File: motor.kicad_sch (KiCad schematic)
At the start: 6 parts, among them IC3 DRV8300DPWR, Q1 Q_NMOS

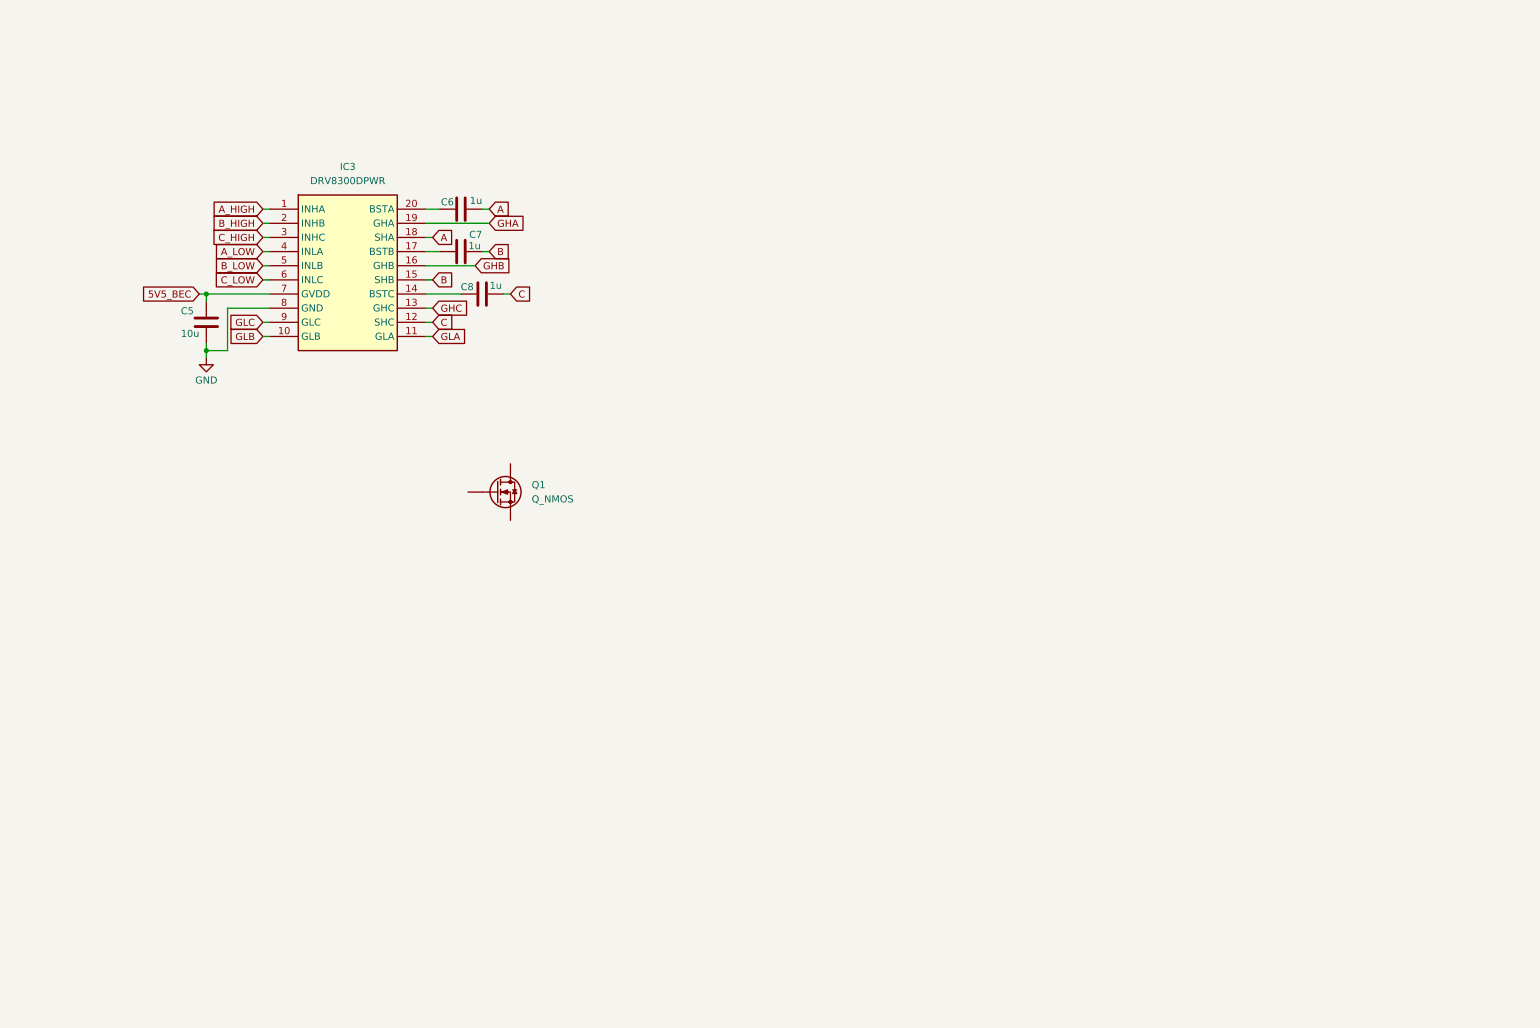
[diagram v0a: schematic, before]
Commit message: finished one full channel, still to duplicate this for 4 channels esc
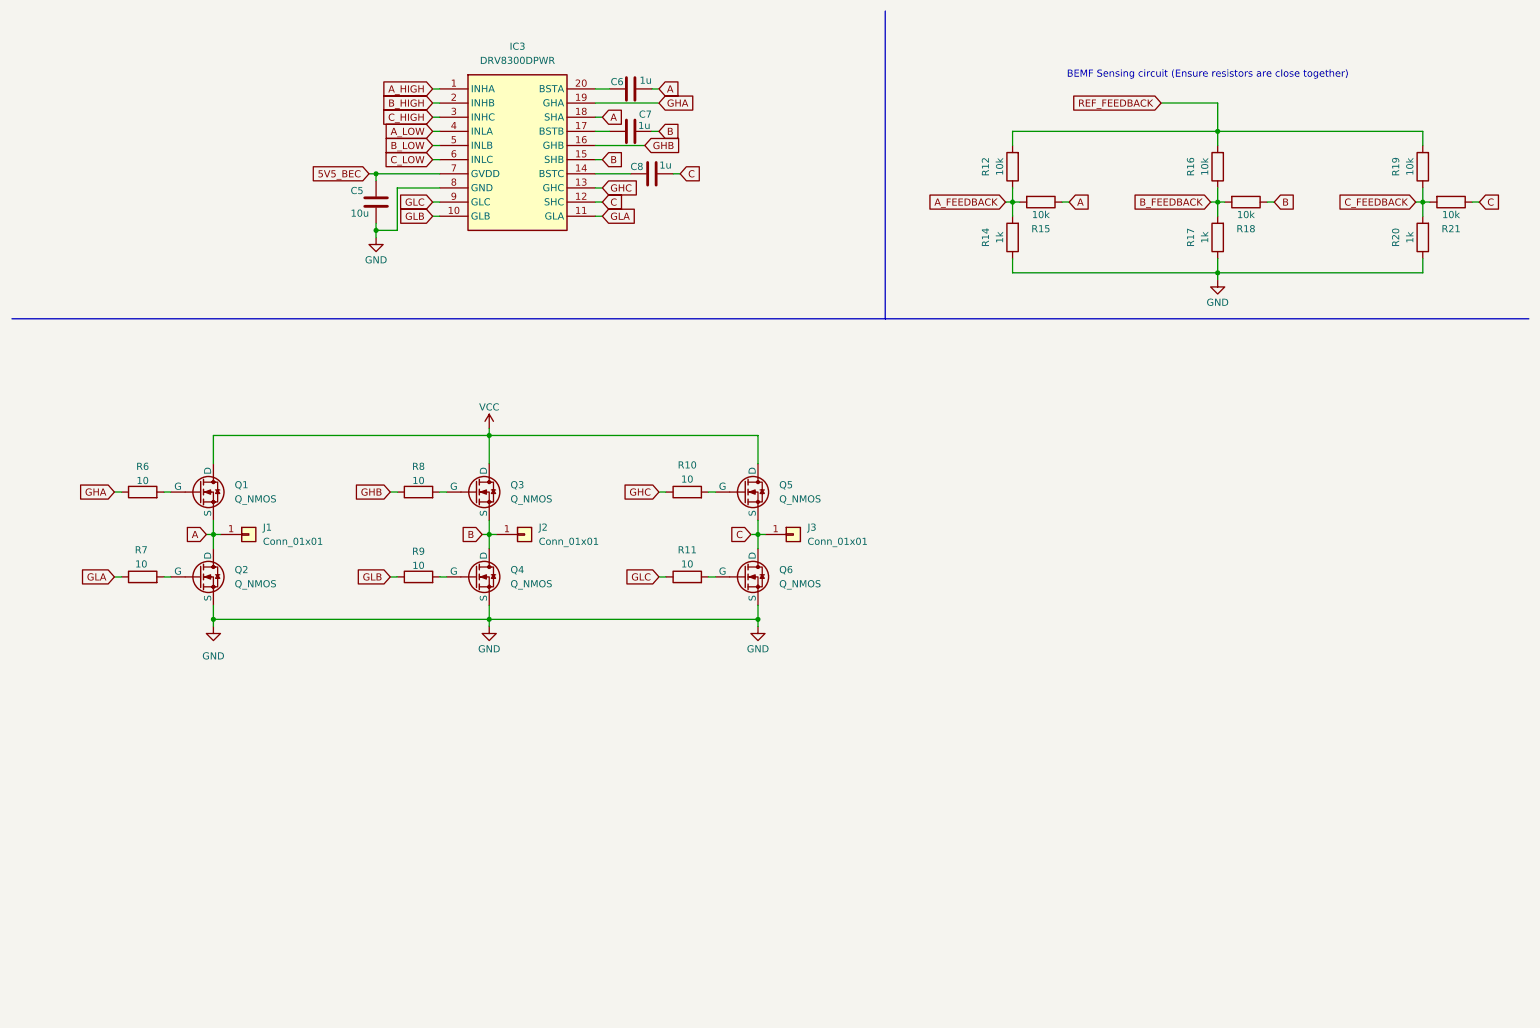
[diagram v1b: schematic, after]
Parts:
- added J1, J2, J3: Conn_01x01, symbol Connector_Generic:Conn_01x01
- added Q2, Q3, Q4, Q5, Q6: Q_NMOS, symbol Device:Q_NMOS
- added R10, R11, R6, R7, R8, R9: 10, symbol Device:R
- added R12, R15, R16, R18, R19, R21: 10k, symbol Device:R
- added R14, R17, R20: 1k, symbol Device:R
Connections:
- net A: now also Q1.S, J1.1 (Pin_1), Q2.D, R15.1
- net B: now also J2.1 (Pin_1), Q3.S, Q4.D, R18.1
- net C: now also J3.1 (Pin_1), Q5.S, Q6.D, R21.1
- net GHA: now also R6.1
- net GHB: now also R8.1
- net GHC: now also R10.1
- net GLA: now also R7.1
- net GLB: now also R9.1
- net GLC: now also R11.1
- net GND: now also Q2.S, Q4.S, Q6.S, R14.1, R17.1, R20.1
- net VCC: now reaches Q1.D
- net VCC: now also Q3.D, Q5.D
- net at Q1.G: now also R6.2
- new net: Q5.G, R10.2
- new net: Q4.G, R9.2
- new net: Q3.G, R8.2
- new net: Q6.G, R11.2
- new net: Q2.G, R7.2
- new net A_FEEDBACK: R12.1, R14.2, R15.2
- new net B_FEEDBACK: R16.1, R17.2, R18.2
- new net C_FEEDBACK: R19.1, R20.2, R21.2
- new net REF_FEEDBACK: R12.2, R16.2, R19.2
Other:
- note added: "BEMF Sensing circuit (Ensure resistors are close together)"
- moved on the sheet: C5, C6, C7, C8, IC3

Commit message: duplicate mcu and motor gates circuit
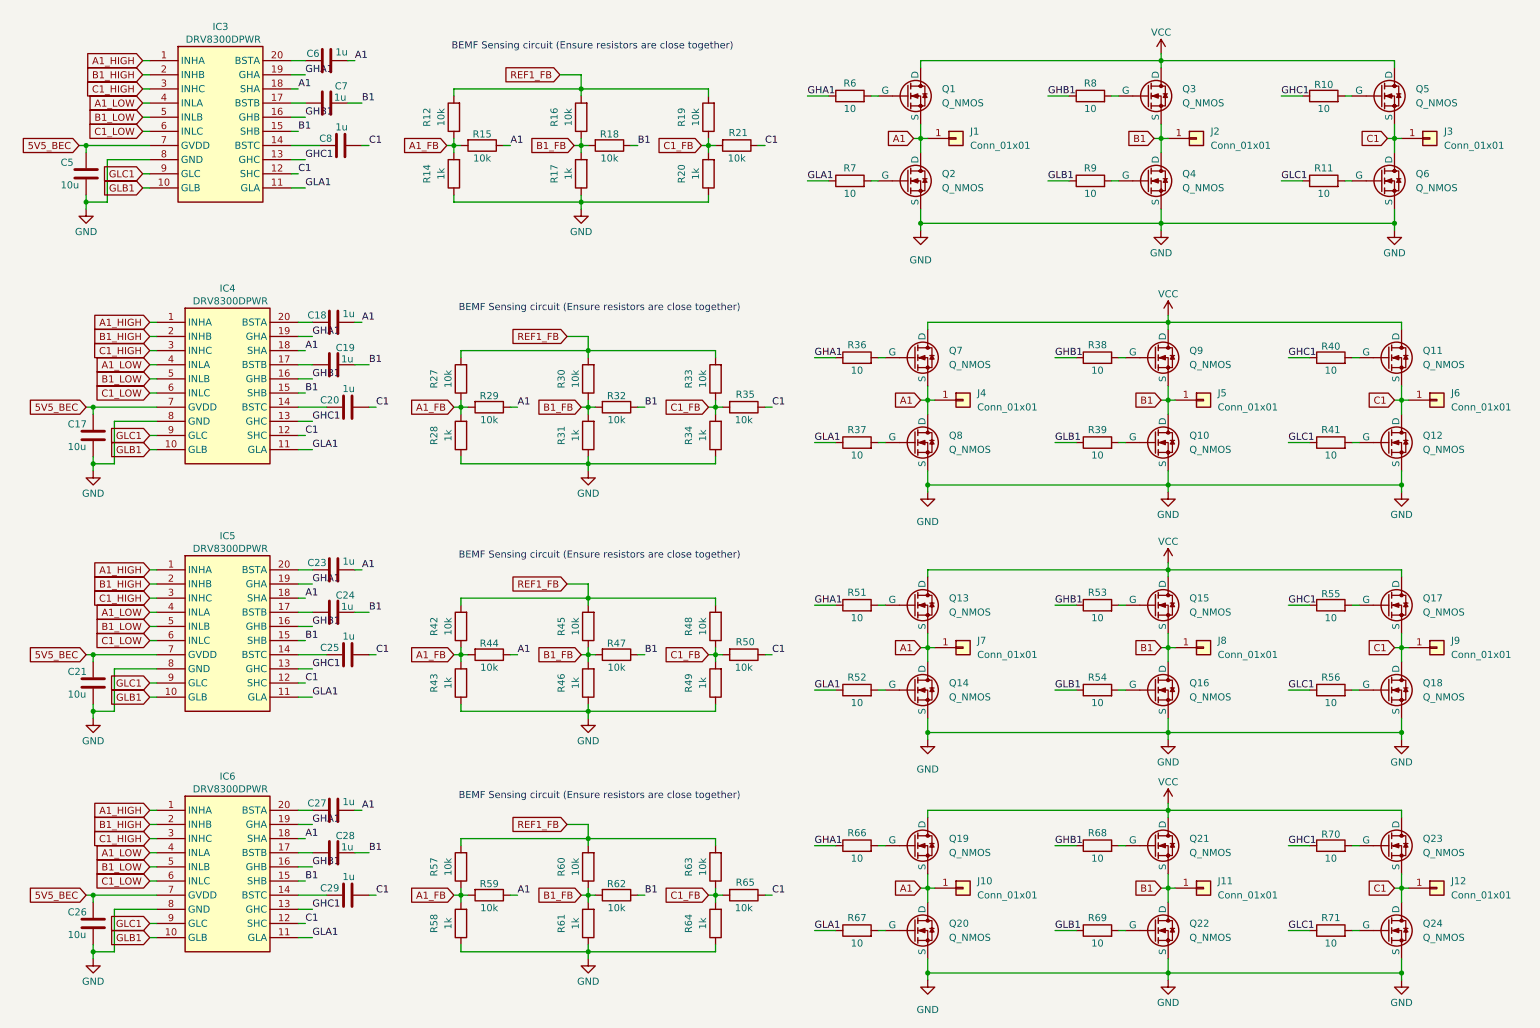
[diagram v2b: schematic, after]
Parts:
- added C17, C21, C26: 10u, symbol Device:C
- added C18, C19, C20, C23, C24, C25, C27, C28, C29: 1u, symbol Device:C
- added IC4, IC5, IC6: DRV8300DPWR, ESCs:SOP65P640X120-20M, symbol ESCs:DRV8300DPWR
- added J10, J11, J12, J4, J5, J6, J7, J8, J9: Conn_01x01, symbol Connector_Generic:Conn_01x01
- added Q10, Q11, Q12, Q13, Q14, Q15, Q16, Q17, Q18, Q19, Q20, Q21, Q22, Q23, Q24, Q7, Q8, Q9: Q_NMOS, symbol Device:Q_NMOS
- added R27, R29, R30, R32, R33, R35, R42, R44, R45, R47, R48, R50, R57, R59, R60, R62, R63, R65: 10k, symbol Device:R
- added R28, R31, R34, R43, R46, R49, R58, R61, R64: 1k, symbol Device:R
- added R36, R37, R38, R39, R40, R41, R51, R52, R53, R54, R55, R56, R66, R67, R68, R69, R70, R71: 10, symbol Device:R
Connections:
- net 5V5_BEC: now also C17.1, C21.1, C26.1, IC4.7 (GVDD), IC5.7 (GVDD), IC6.7 (GVDD)
- net GND: now also C17.2, C21.2, C26.2, IC4.8 (GND), IC5.8 (GND), IC6.8 (GND), Q10.S, Q12.S, Q14.S, Q16.S, Q18.S, Q20.S, Q22.S, Q24.S, Q8.S, R28.1, R31.1, R34.1, R43.1, R46.1, R49.1, R58.1, R61.1, R64.1
- net VCC: now also Q11.D, Q13.D, Q15.D, Q17.D, Q19.D, Q21.D, Q23.D, Q7.D, Q9.D
- net A renamed A1
- net A1: now also C18.2, C23.2, C27.2, IC4.18 (SHA), IC5.18 (SHA), IC6.18 (SHA), J10.1 (Pin_1), J4.1 (Pin_1), J7.1 (Pin_1), Q13.S, Q14.D, Q19.S, Q20.D, Q7.S, Q8.D, R29.1, R44.1, R59.1
- net A_FEEDBACK renamed A1_FB
- net A1_FB: now also R27.1, R28.2, R29.2, R42.1, R43.2, R44.2, R57.1, R58.2, R59.2
- net A_HIGH renamed A1_HIGH
- net A1_HIGH: now also IC4.1 (INHA), IC5.1 (INHA), IC6.1 (INHA)
- net A_LOW renamed A1_LOW
- net A1_LOW: now also IC4.4 (INLA), IC5.4 (INLA), IC6.4 (INLA)
- net B renamed B1
- net B1: now also C19.2, C24.2, C28.2, IC4.15 (SHB), IC5.15 (SHB), IC6.15 (SHB), J11.1 (Pin_1), J5.1 (Pin_1), J8.1 (Pin_1), Q10.D, Q15.S, Q16.D, Q21.S, Q22.D, Q9.S, R32.1, R47.1, R62.1
- net B_FEEDBACK renamed B1_FB
- net B1_FB: now also R30.1, R31.2, R32.2, R45.1, R46.2, R47.2, R60.1, R61.2, R62.2
- net B_HIGH renamed B1_HIGH
- net B1_HIGH: now also IC4.2 (INHB), IC5.2 (INHB), IC6.2 (INHB)
- net B_LOW renamed B1_LOW
- net B1_LOW: now also IC4.5 (INLB), IC5.5 (INLB), IC6.5 (INLB)
- net C renamed C1
- net C1: now also C20.2, C25.2, C29.2, IC4.12 (SHC), IC5.12 (SHC), IC6.12 (SHC), J12.1 (Pin_1), J6.1 (Pin_1), J9.1 (Pin_1), Q11.S, Q12.D, Q17.S, Q18.D, Q23.S, Q24.D, R35.1, R50.1, R65.1
- net C_FEEDBACK renamed C1_FB
- net C1_FB: now also R33.1, R34.2, R35.2, R48.1, R49.2, R50.2, R63.1, R64.2, R65.2
- net C_HIGH renamed C1_HIGH
- net C1_HIGH: now also IC4.3 (INHC), IC5.3 (INHC), IC6.3 (INHC)
- net C_LOW renamed C1_LOW
- net C1_LOW: now also IC4.6 (INLC), IC5.6 (INLC), IC6.6 (INLC)
- net GHA renamed GHA1
- net GHA1: now also IC4.19 (GHA), IC5.19 (GHA), IC6.19 (GHA), R36.1, R51.1, R66.1
- net GHB renamed GHB1
- net GHB1: now also IC4.16 (GHB), IC5.16 (GHB), IC6.16 (GHB), R38.1, R53.1, R68.1
- net GHC renamed GHC1
- net GHC1: now also IC4.13 (GHC), IC5.13 (GHC), IC6.13 (GHC), R40.1, R55.1, R70.1
- net GLA renamed GLA1
- net GLA1: now also IC4.11 (GLA), IC5.11 (GLA), IC6.11 (GLA), R37.1, R52.1, R67.1
- net GLB renamed GLB1
- net GLB1: now also IC4.10 (GLB), IC5.10 (GLB), IC6.10 (GLB), R39.1, R54.1, R69.1
- net GLC renamed GLC1
- net GLC1: now also IC4.9 (GLC), IC5.9 (GLC), IC6.9 (GLC), R41.1, R56.1, R71.1
- net REF_FEEDBACK renamed REF1_FB
- net REF1_FB: now also R27.2, R30.2, R33.2, R42.2, R45.2, R48.2, R57.2, R60.2, R63.2
- new net: Q15.G, R53.2
- new net: C19.1, IC4.17 (BSTB)
- new net: Q20.G, R67.2
- new net: Q19.G, R66.2
- new net: Q10.G, R39.2
- new net: Q9.G, R38.2
- new net: Q22.G, R69.2
- new net: Q23.G, R70.2
- new net: Q7.G, R36.2
- new net: Q8.G, R37.2
- new net: Q12.G, R41.2
- new net: Q24.G, R71.2
- new net: C29.1, IC6.14 (BSTC)
- new net: C28.1, IC6.17 (BSTB)
- new net: C27.1, IC6.20 (BSTA)
- new net: C18.1, IC4.20 (BSTA)
- new net: Q17.G, R55.2
- new net: C25.1, IC5.14 (BSTC)
- new net: C24.1, IC5.17 (BSTB)
- new net: C23.1, IC5.20 (BSTA)
- new net: C20.1, IC4.14 (BSTC)
- new net: Q21.G, R68.2
- new net: Q13.G, R51.2
- new net: Q14.G, R52.2
- new net: Q18.G, R56.2
- new net: Q16.G, R54.2
- new net: Q11.G, R40.2
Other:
- moved on the sheet: C5, C6, C7, C8, IC3, J1, J2, J3, Q1, Q2, Q3, Q4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
